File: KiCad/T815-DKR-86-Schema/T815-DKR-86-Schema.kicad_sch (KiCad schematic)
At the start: 43 parts, among them M1 RC Model Motor, Q1 BC337, Q2 BC337, Q4 BC337, Q5 BC337, Q6 BC337, U1 Optocoupler_Module, U2 Optocoupler_Module, U3 PWM_MOSFET_Module, U4 ESC - regulator, U5 Step Down to 5V

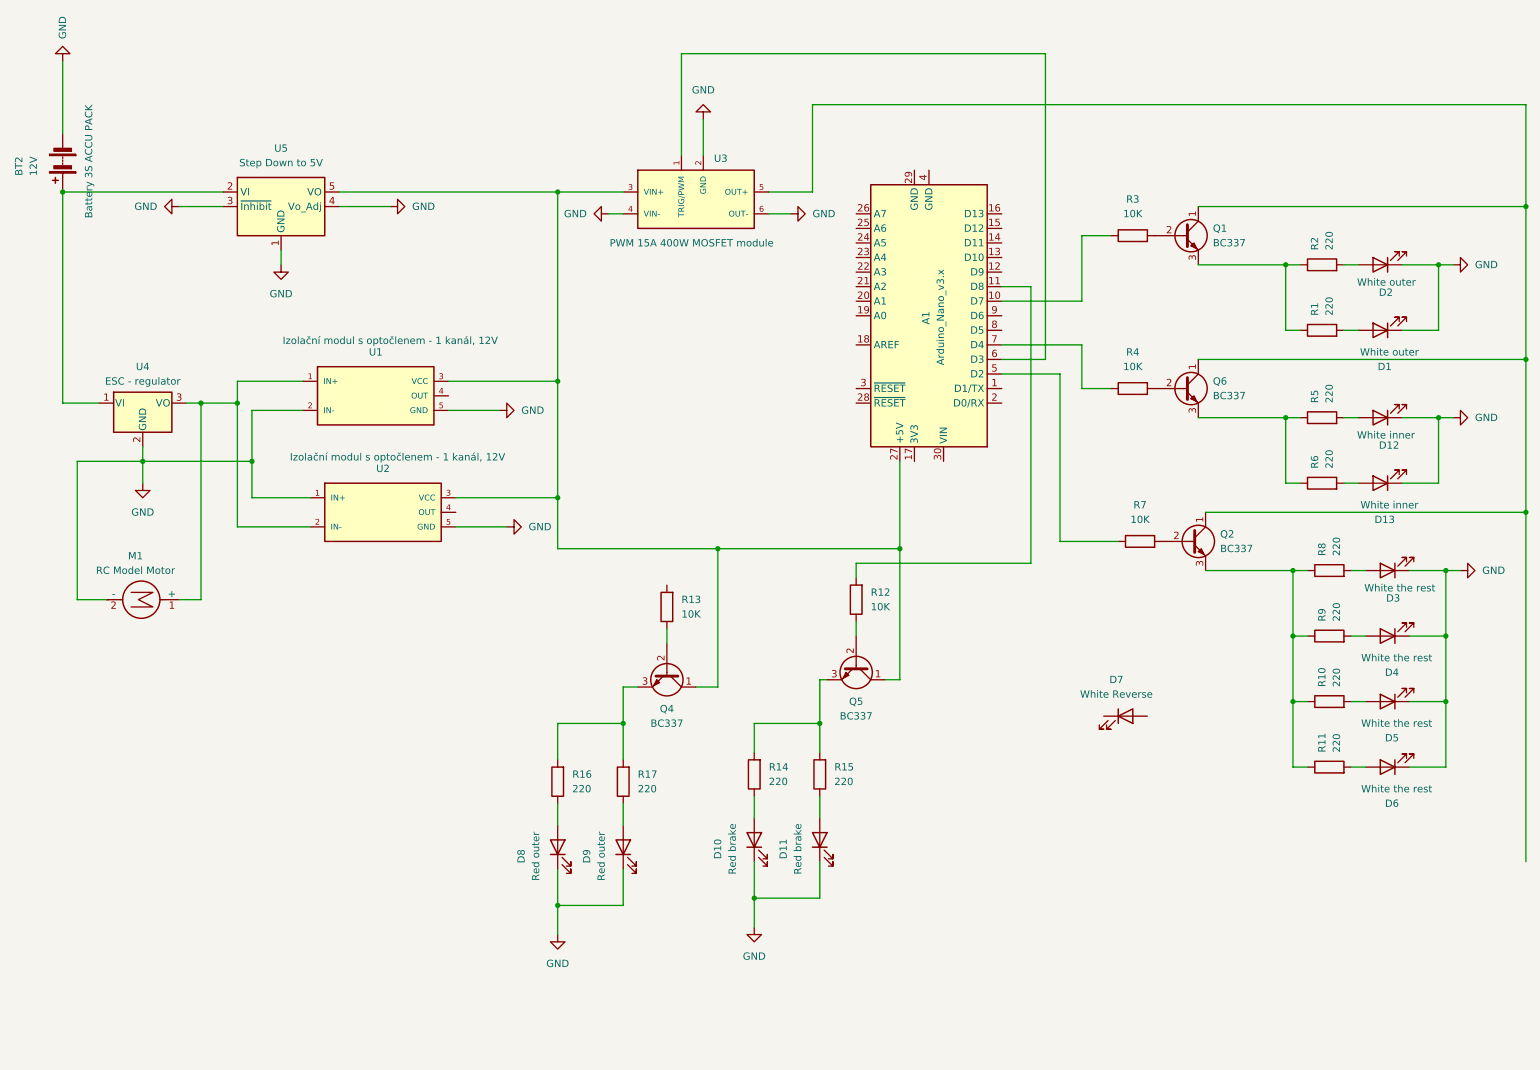
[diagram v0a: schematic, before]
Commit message: Relevant version using mosfets.
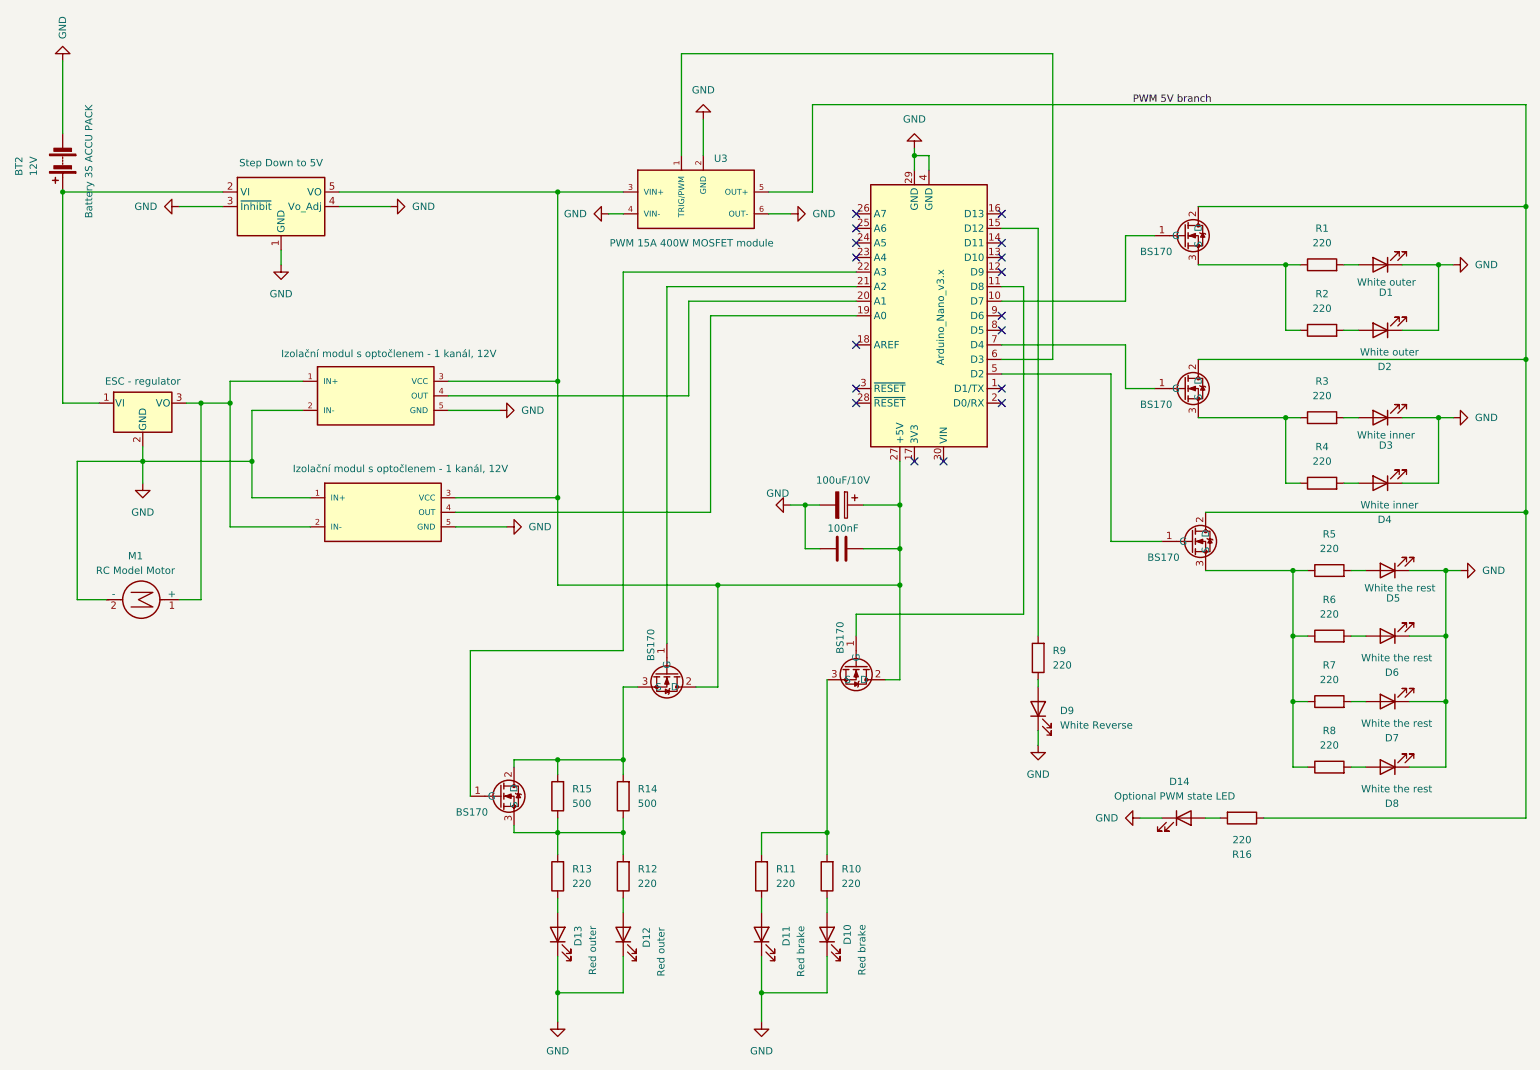
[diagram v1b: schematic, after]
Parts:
- removed Q1, Q2, Q4, Q5, Q6: BC337, Package_TO_SOT_THT:TO-92_Inline, symbol Transistor_BJT:BC337
- removed R12, R13, R3, R4, R7: 10K, symbol Device:R
- added C1: 100uF/10V, symbol Device:C_Polarized
- added C2: 100nF, symbol Device:C
- added D14: Optional PWM state LED, symbol Device:LED
- added Q10, Q11, Q3, Q7, Q8, Q9: BS170, Package_TO_SOT_THT:TO-220-3_Vertical, symbol Transistor_FET:IRLZ44N
- added R14, R15: 500, symbol Device:R
- added R16, R9: 220, symbol Device:R
- renumbered D2 to D1, D11 to D10, D10 to D11, D9 to D12, D8 to D13, D1 to D2, D12 to D3, D13 to D4, D3 to D5, D4 to D6, D5 to D7, D6 to D8, D7 to D9, R2 to R1, R15 to R10, R14 to R11, R17 to R12, R16 to R13, R1 to R2, R5 to R3, R6 to R4, R8 to R5, R9 to R6, R10 to R7, R11 to R8
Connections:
- net GND: now also A1.29 (GND), A1.4 (GND), D9.1 (K), C1.2, C2.1, D14.1 (K)
- net at R12.2, R13.2: now also Q3.3 (S), R14.1, R15.1
- net at A1.27 (+5V), U1.3 (VCC), U2.3 (VCC)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: now also C1.1, C2.2, Q7.2 (D), Q8.2 (D)
- net at U2.4 (OUT): now also A1.19 (A0)
- net at R5.1, R6.1, R7.1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: now also Q9.3 (S)
- net at U1.4 (OUT): now also A1.20 (A1)
- net at A1.7 (D4): now also Q10.1 (G)
- net at R1.1, R2.1: now also Q11.3 (S)
- net at A1.5 (D2): now also Q9.1 (G)
- net at R10.2, R11.2: now also Q8.3 (S)
- net at D9.2 (A): now also R9.1
- net at R3.1, R4.1: now also Q10.3 (S)
- net PWM 5V branch: now reaches U3.5 (OUT+)
- net PWM 5V branch: now also Q10.2 (D), Q11.2 (D), Q9.2 (D), R16.1
- net at A1.10 (D7): now also Q11.1 (G)
- net at A1.11 (D8): now also Q8.1 (G)
- net at A1.15 (D12): now also R9.2
- net at A1.21 (A2): now also Q7.1 (G)
- net at A1.22 (A3): now also Q3.1 (G)
- new net: Q3.2 (D), Q7.3 (S), R14.2, R15.2
- new net: D14.2 (A), R16.2
- no-connect marks 0 -> 17
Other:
- company: (none) -> Petr Škaloud
- title: (none) -> Lighting module for RC Tatra T815 Dakar 1986
- moved on the sheet: D10, D11, D12, D13, D9, R10, R11, R12, R13
